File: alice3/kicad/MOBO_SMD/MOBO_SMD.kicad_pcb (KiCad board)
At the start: 2 copper layers, 74.9 x 114.3 mm, 40 parts, among them CON1 SD_Card, P1 CONN_01X05, P2 CONN_01X01, SW1 RESET, SW2 SOFT RESET, U2 VGA_daughter_board, U3 Propeller_P8X32A-D40, U4 24LC256, U5 Propeller_Plug, U6 MiniM4-D40, U8 Z80CPU, U9 KM681000BLP-7, Y1 5 MHz

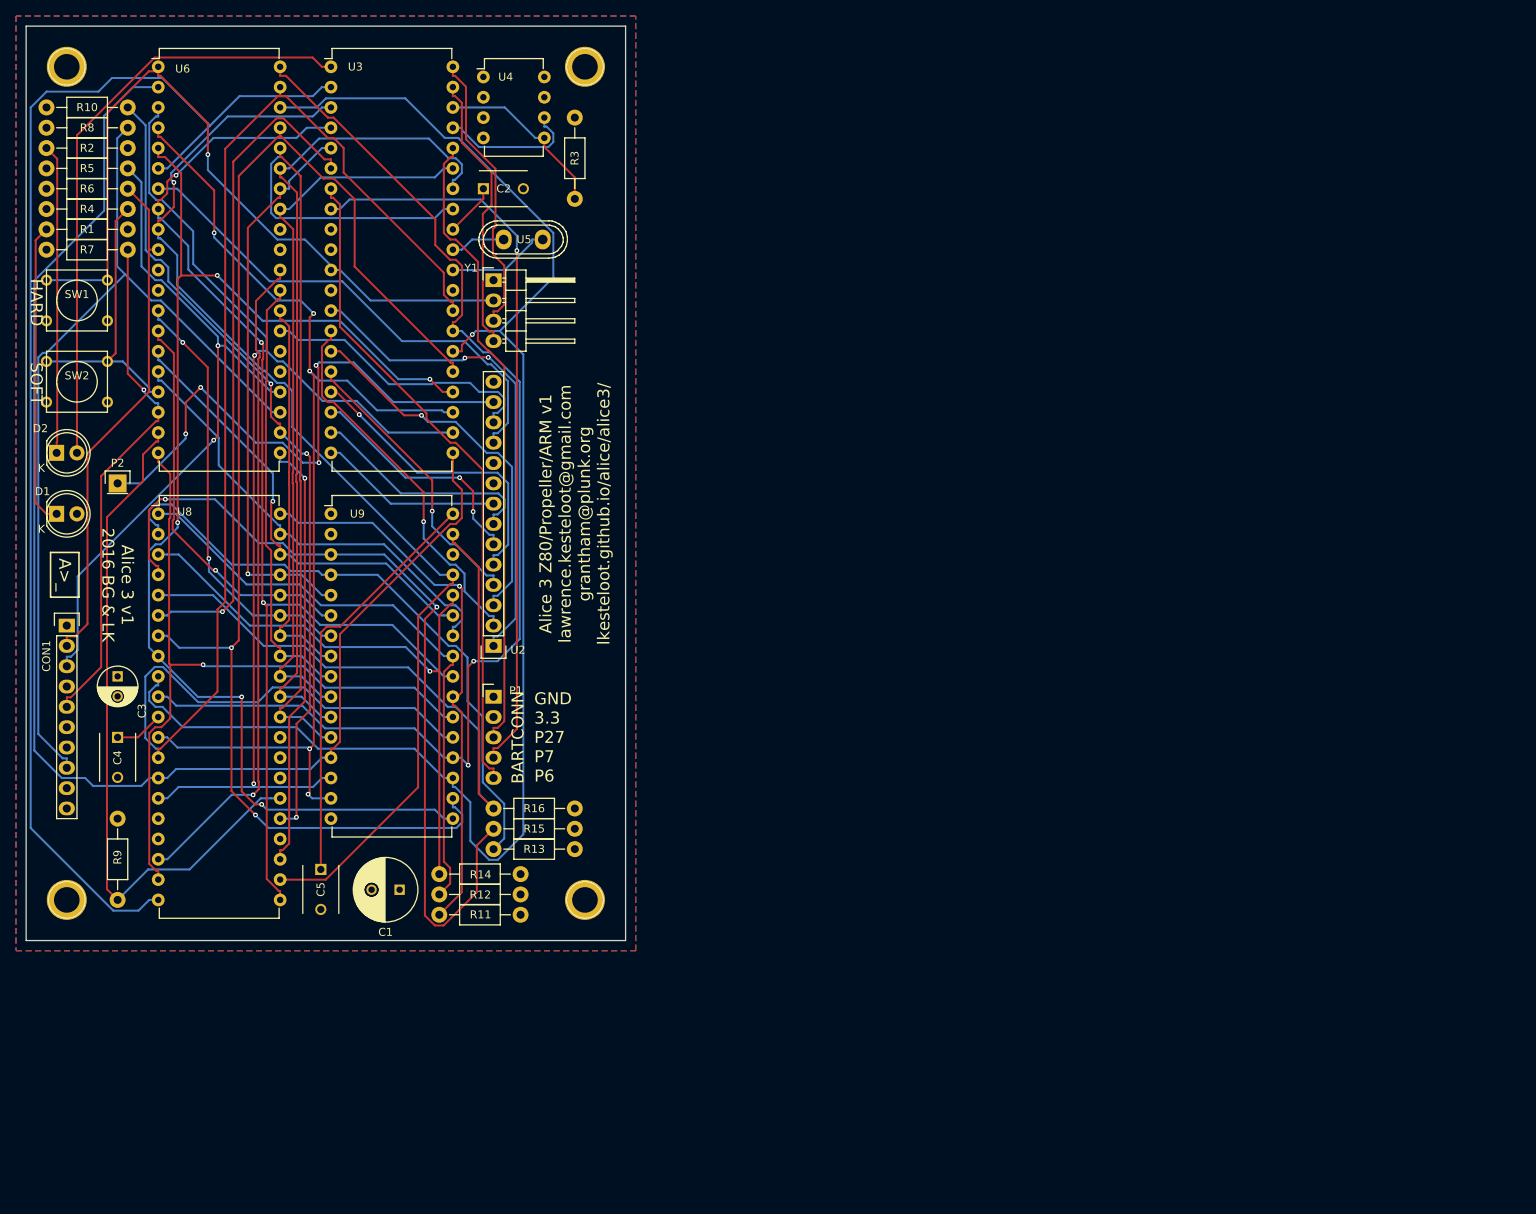
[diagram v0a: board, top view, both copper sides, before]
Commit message: Stab at full PCB
replace DIP36 128KB RAM with TSOP44 512KB RAM
change footprints for many components to SMD
sample PCB layout
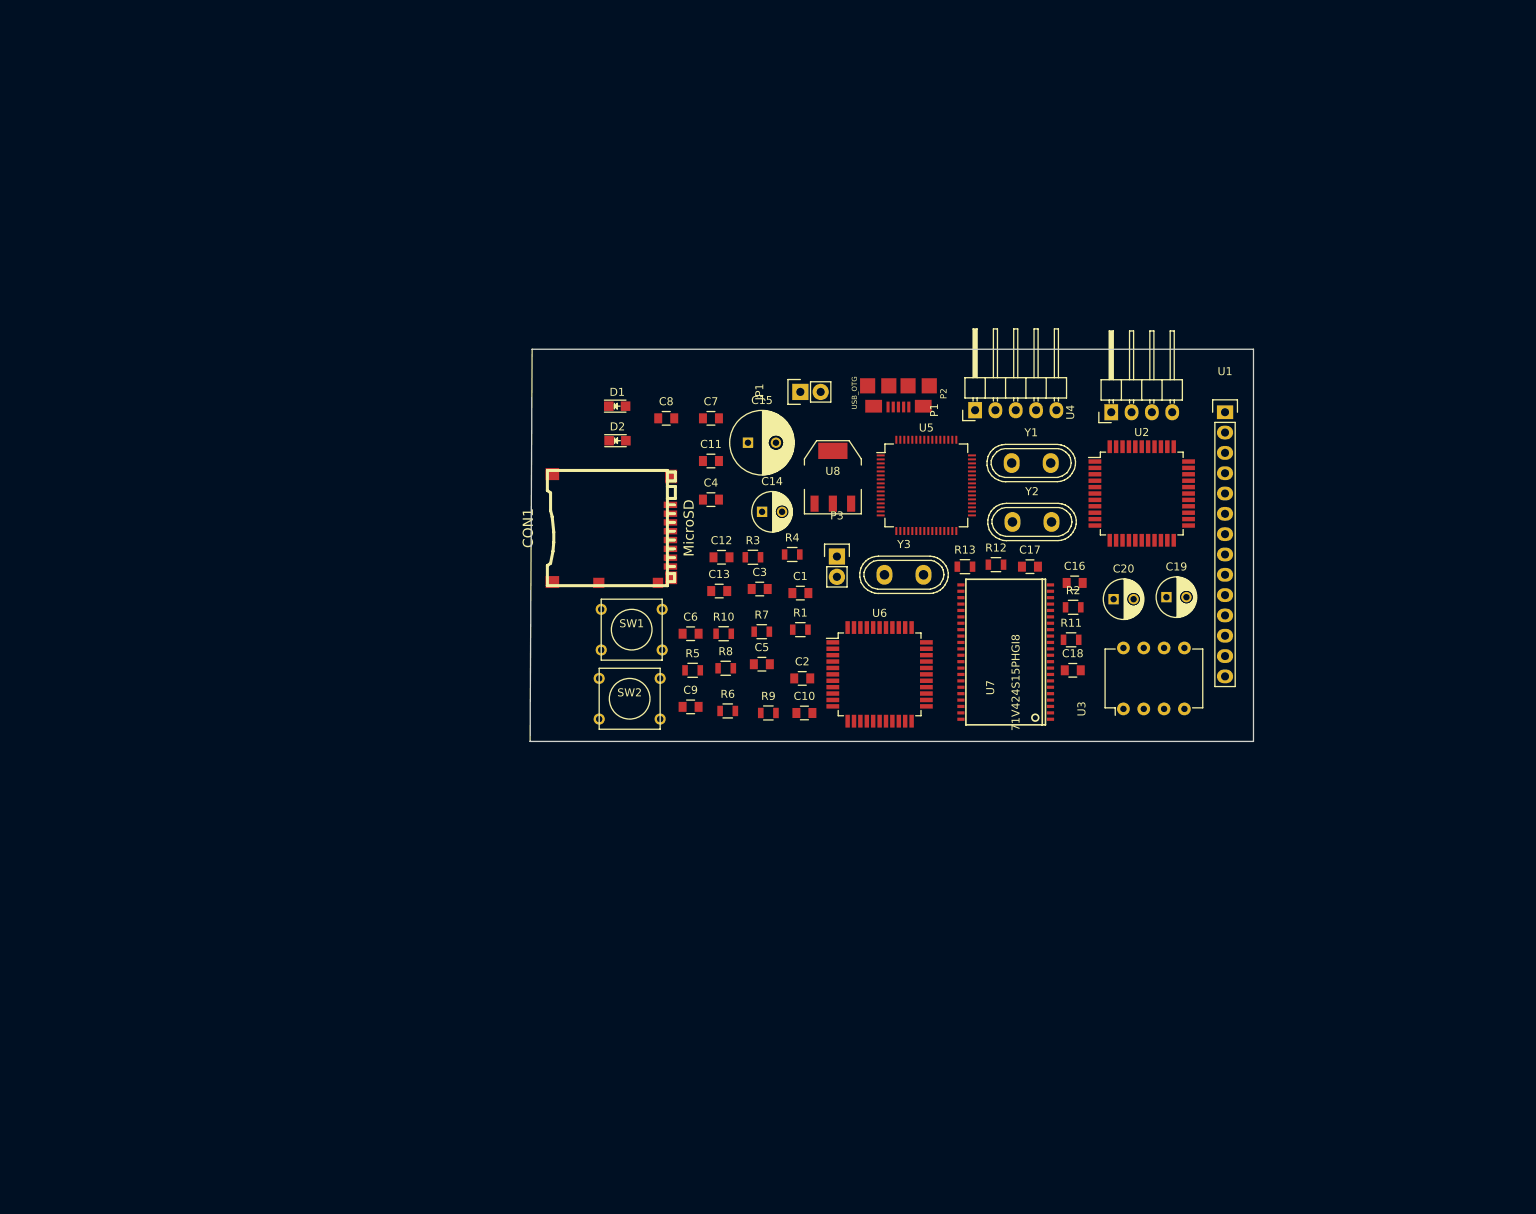
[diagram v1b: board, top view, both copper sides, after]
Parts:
- removed HOLE1, HOLE2, HOLE3, HOLE4: 1pin, Connect:1pin
- removed R14, R15, R16: 10k, Resistors_ThroughHole:Resistor_Horizontal_RM10mm
- removed U9: KM681000BLP-7, Housings_DIP:DIP-32_W15.24mm
- added C10: 2.2µF, Capacitors_SMD:C_0805, F.Cu at (143.0, 118.9)
- added C11: 2.2µF, Capacitors_SMD:C_0805, F.Cu at (131.3, 87.4)
- added C12: 22pF, Capacitors_SMD:C_0805, F.Cu at (132.6, 99.4)
- added C13: 22pF, Capacitors_SMD:C_0805, F.Cu at (132.3, 103.6)
- added C14: 10µF, Capacitors_ThroughHole:C_Radial_D5_L11_P2.5, F.Cu at (137.7, 93.7)
- added C15: 1000 µF, Capacitors_ThroughHole:C_Radial_D8_L11.5_P3.5, F.Cu at (135.9, 85.1)
- added C16: 0.1 µF, Capacitors_SMD:C_0805, F.Cu at (176.8, 102.6)
- added C17: 0.1 µF, Capacitors_SMD:C_0805, F.Cu at (171.2, 100.6)
- added C18: 0.1 µF, Capacitors_SMD:C_0805, F.Cu at (176.5, 113.5)
- added C19: 10µF, Capacitors_ThroughHole:C_Radial_D5_L11_P2.5, F.Cu at (188.3, 104.4)
- added C20: 10µF, Capacitors_ThroughHole:C_Radial_D5_L11_P2.5, F.Cu at (181.7, 104.6)
- added C6: 22pF, Capacitors_SMD:C_0805, F.Cu at (128.8, 109.0)
- added C7: 100nF, Capacitors_SMD:C_0805, F.Cu at (131.3, 82.0)
- added C8: 100nF, Capacitors_SMD:C_0805, F.Cu at (125.7, 82.0)
- added C9: 100nF, Capacitors_SMD:C_0805, F.Cu at (128.8, 118.1)
- added JP1: Jumper_NO_Small, Pin_Headers:Pin_Header_Straight_1x02, F.Cu at (142.5, 78.7)
- added P3: UART1, Pin_Headers:Pin_Header_Straight_1x02, F.Cu at (147.1, 99.3)
- added U1: VGA_daughter_board, Pin_Headers:Pin_Header_Straight_1x14, F.Cu at (195.6, 81.3)
- added U7: 71V424S15PHGI8, TSOP44-II:TSOP44-II, F.Cu at (168.2, 111.3)
- added Y2: 16MHz, Crystals:Crystal_HC50-U_Vertical, F.Cu at (171.4, 95.0)
- added Y3: 32.768KHz, Crystals:Crystal_HC50-U_Vertical, F.Cu at (155.4, 101.6)
- C1: value 1000 µF -> 0.1 µF; footprint Capacitors_ThroughHole:C_Radial_D8_L11.5_P3.5 -> Capacitors_SMD:C_0805
- C2, C4: value 0.1 µF -> 100nF; footprint Capacitors_ThroughHole:C_Disc_D6_P5 -> Capacitors_SMD:C_0805
- C3: value 10µF -> 100nF; footprint Capacitors_ThroughHole:C_Radial_D5_L11_P2.5 -> Capacitors_SMD:C_0805
- C5: value 0.1 µF -> 22pF; footprint Capacitors_ThroughHole:C_Disc_D6_P5 -> Capacitors_SMD:C_0805
- CON1: value SD_Card -> MicroSD; footprint Pin_Headers:Pin_Header_Straight_1x10 -> microsd:microsd_socket
- D1: value POWER -> DEBUG; footprint LEDs:LED-5MM -> LEDs:LED_0805
- D2: value DEBUG -> POWER; footprint LEDs:LED-5MM -> LEDs:LED_0805
- P2: value CONN_01X01 -> USB_OTG; footprint Pin_Headers:Pin_Header_Straight_1x01 -> microusb:10118192-0001LF
- R1, R13, R3, R6, R7, R8: footprint Resistors_ThroughHole:Resistor_Horizontal_RM10mm -> Resistors_SMD:R_0805
- R10: value 1k -> 100; footprint Resistors_ThroughHole:Resistor_Horizontal_RM10mm -> Resistors_SMD:R_0805
- R11, R12: value 10k -> 1k; footprint Resistors_ThroughHole:Resistor_Horizontal_RM10mm -> Resistors_SMD:R_0805
- R2: value 100 -> 10k; footprint Resistors_ThroughHole:Resistor_Horizontal_RM10mm -> Resistors_SMD:R_0805
- R4: value 10k -> 220; footprint Resistors_ThroughHole:Resistor_Horizontal_RM10mm -> Resistors_SMD:R_0805
- R5: value 68K -> 10k; footprint Resistors_ThroughHole:Resistor_Horizontal_RM10mm -> Resistors_SMD:R_0805
- R9: value 1k -> 68K; footprint Resistors_ThroughHole:Resistor_Horizontal_RM10mm -> Resistors_SMD:R_0805
- U2: value VGA_daughter_board -> Propeller_P8X32A-D40; footprint Pin_Headers:Pin_Header_Straight_1x14 -> Housings_QFP:LQFP-44_10x10mm_Pitch0.8mm
- U3: value Propeller_P8X32A-D40 -> 24LC256; footprint Housings_DIP:DIP-40_W15.24mm -> Housings_DIP:DIP-8_W7.62mm
- U4: value 24LC256 -> Propeller_Plug; footprint Housings_DIP:DIP-8_W7.62mm -> Pin_Headers:Pin_Header_Angled_1x04
- U5: value Propeller_Plug -> STM32F415RG; footprint Pin_Headers:Pin_Header_Angled_1x04 -> Housings_QFP:LQFP-64_10x10mm_Pitch0.5mm
- U6: value MiniM4-D40 -> Z80CPU; footprint Housings_DIP:DIP-40_W15.24mm -> Housings_QFP:LQFP-44_10x10mm_Pitch0.8mm
- U8: value Z80CPU -> LD29080DT33R; footprint Housings_DIP:DIP-40_W15.24mm -> TO_SOT_Packages_SMD:SOT-223
- moved R2 136.0 mm to (176.6, 105.7)
- moved U3 127.5 mm to (182.9, 118.4), turned to 90 degrees
- moved U6 117.9 mm to (152.4, 114.0)
- moved R8 104.6 mm to (133.2, 113.3)
- moved R6 103.3 mm to (133.4, 118.6)
- moved R10 103.2 mm to (132.9, 109.0)
- moved R1 102.2 mm to (142.5, 108.5)
- moved P2 98.6 mm to (154.8, 76.5), turned to 180 degrees
- moved R5 98.3 mm to (129.0, 113.5)
- moved R4 98.1 mm to (141.5, 99.1), turned to 0 degrees
- moved R7 96.9 mm to (137.7, 108.7)
- moved U4 89.0 mm to (181.4, 81.3), turned to 90 degrees
- moved U8 84.5 mm to (146.6, 89.4)
- moved R9 83.4 mm to (138.5, 118.9), turned to 0 degrees
- moved U2 83.2 mm to (185.2, 91.4), turned to 0 degrees
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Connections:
- C2 pad 1: +3V3 -> GND
- C2 pad 2: GND -> +3V3
- C3 pad 1: +3V3 -> GND
- C3 pad 2: GND -> +3V3
- C4 pad 1: +3V3 -> GND
- C4 pad 2: GND -> +3V3
- C5 pad 1: +3V3 -> Net-(C5-Pad1)
- CON1 pad 4: Net-(CON1-Pad4) -> +3V3
- CON1 pad 6: +3V3 -> GND
- CON1 pad 7: GND -> /IO/DO
- CON1 pad 8: /IO/DO -> Net-(CON1-Pad8)
- D1 pad 2: +3V3 -> Net-(D1-Pad2)
- D2 pad 2: Net-(D2-Pad2) -> +3V3
- R10 pad 1: +3V3 -> Net-(D2-Pad1)
- R10 pad 2: /BUSRQ -> GND
- R11 pad 1: GND -> /Z80_RESET
- R11 pad 2: A10 -> GND
- R12 pad 1: GND -> +3V3
- R12 pad 2: A11 -> /BUSRQ
- R13 pad 2: A12 -> A16
- R2 pad 1: Net-(D2-Pad1) -> +3V3
- R2 pad 2: GND -> Net-(R2-Pad2)
- R3 pad 2: Net-(R3-Pad2) -> Net-(JP1-Pad1)
- R4 pad 1: Net-(R4-Pad1) -> USB_DET
- R4 pad 2: GND -> +5V
- R5 pad 1: +3V3 -> Net-(R5-Pad1)
- R5 pad 2: /IO/DI -> GND
- R6 pad 2: /IO/CS -> /IO/DO
- R8 pad 2: /IO/DO -> /IO/DI
- R9 pad 1: /Z80_RESET -> +3V3
- R9 pad 2: GND -> /IO/CS
- SW2 pad 1: Net-(R4-Pad1) -> Net-(R5-Pad1)
- U2 pad 1: Net-(U2-Pad1) -> Net-(D1-Pad2)
- U2 pad 10: Net-(U2-Pad10) -> GND
- U2 pad 11: KBD_DATA -> /RESET
- U2 pad 12: KBD_CLK -> +3V3
- U2 pad 13: +5V -> Net-(U1-Pad1)
- U2 pad 14: GND -> Net-(U1-Pad2)
- U2 pad 2: Net-(U2-Pad2) -> /IORQ
- U2 pad 3: Net-(U2-Pad3) -> /WR
- U2 pad 4: Net-(U2-Pad4) -> /RD
- U2 pad 5: Net-(U2-Pad5) -> A7
- U2 pad 6: Net-(U2-Pad6) -> CLK
- U2 pad 7: Net-(U2-Pad7) -> Net-(P1-Pad5)
- U2 pad 8: Net-(U2-Pad8) -> Net-(P1-Pad4)
- U2 pad 9: Net-(U2-Pad9) -> GND
- U3 pad 1: Net-(D2-Pad2) -> GND
- U3 pad 2: /IORQ -> GND
- U3 pad 3: /WR -> GND
- U3 pad 4: /RD -> GND
- U3 pad 5: A7 -> Net-(R2-Pad2)
- U3 pad 6: CLK -> Net-(U2-Pad37)
- U3 pad 7: Net-(P1-Pad5) -> GND
- U3 pad 8: Net-(P1-Pad4) -> +3V3
- U4 pad 2: GND -> /RESET
- U4 pad 3: GND -> Net-(U2-Pad40)
- U4 pad 4: GND -> Net-(U2-Pad39)
- U5 pad 1: GND -> +3V3
- U5 pad 2: /RESET -> A10
- U5 pad 3: Net-(U3-Pad40) -> Net-(C12-Pad1)
- U5 pad 4: Net-(U3-Pad39) -> Net-(C13-Pad2)
- U6 pad 1: /RESET -> A11
- U6 pad 10: /IO/CS -> D6
- U6 pad 12: GND -> D2
- U6 pad 13: A5 -> D7
- U6 pad 14: A6 -> D0
- U6 pad 15: A8 -> D1
- U6 pad 16: A9 -> +3V3
- U6 pad 17: Net-(R4-Pad1) -> +3V3
- U6 pad 18: /IO/SCK -> /HALT
- U6 pad 19: /Z80_RESET -> /MREQ
- U6 pad 2: D0 -> A12
- U6 pad 20: /MREQ -> /IORQ
- U6 pad 21: /BUSACK -> /RD
- U6 pad 22: /BUSRQ -> /WR
- U6 pad 23: /IO/DO -> /BUSACK
- U6 pad 24: /IO/DI -> +3V3
- U6 pad 25: Net-(U6-Pad25) -> /BUSRQ
- U6 pad 26: Net-(U6-Pad26) -> /Z80_RESET
- U6 pad 27: KBD_CLK -> Net-(U6-Pad27)
- U6 pad 28: A4 -> Net-(U6-Pad28)
- U6 pad 29: A3 -> GND
- U6 pad 3: D1 -> A13
- U6 pad 30: /HALT -> A0
- U6 pad 31: GND -> A1
- U6 pad 32: +3V3 -> A2
- U6 pad 33: A2 -> A3
- U6 pad 34: A7 -> A4
- U6 pad 35: A1 -> A5
- U6 pad 36: A0 -> A6
- U6 pad 37: D4 -> A7
- U6 pad 38: D5 -> A8
- U6 pad 39: D7 -> A9
- U6 pad 4: D2 -> A14
- U6 pad 40: D6 -> A10
- U6 pad 5: D3 -> A15
- U6 pad 6: /IORQ -> CLK
- U6 pad 7: KBD_DATA -> D4
- U6 pad 8: /RD -> D3
- U6 pad 9: /WR -> D5
- U8 pad 1: A11 -> +5V
- U8 pad 2: A12 -> GND
- U8 pad 3: A13 -> +3V3
- U8 pad 4: A14 -> (no net)
- Y1 pad 1: Net-(U3-Pad30) -> Net-(U2-Pad30)
- Y1 pad 2: Net-(U3-Pad31) -> Net-(U2-Pad31)
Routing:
- net D5: track 191.6 -> 0.00 mm, vias 1 -> 0
- net D7: track 182.3 -> 0.00 mm
- net D0: track 177.5 -> 0.00 mm
- net D4: track 169.5 -> 0.00 mm, vias 2 -> 0
- net /IORQ: track 163.0 -> 0.00 mm
- net D3: track 160.0 -> 0.00 mm, vias 5 -> 0
- net D6: track 150.1 -> 0.00 mm, vias 2 -> 0
- net /RD: track 147.9 -> 0.00 mm, vias 3 -> 0
- net D1: track 143.4 -> 0.00 mm, vias 2 -> 0
- net /WR: track 142.3 -> 0.00 mm, vias 1 -> 0
- net D2: track 136.6 -> 0.00 mm, vias 5 -> 0
- net /IO/DO: track 114.2 -> 0.00 mm
- net A0: track 113.2 -> 0.00 mm
- net A14: track 107.5 -> 0.00 mm, vias 2 -> 0
- net A1: track 104.8 -> 0.00 mm
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- removed copper zone on F.Cu, net +3V3
- removed copper zone on B.Cu, net GND
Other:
- board size 74.9 x 114.3 mm -> 90.4 x 49 mm
- board text removed: "A>_"
- board text removed: "Alice 3 Z80/Propeller/ARM v1 lawrence.kesteloot@gmail.com grantham@plunk.org lkesteloot.github.io/alice/alice3/"
- board text removed: "Alice 3 v1 2016 BG & LK"
- board text removed: "BARTCONN"
- board text removed: "GND 3.3 P27 P7 P6"
- board text removed: "HARD"
- board text removed: "SOFT"

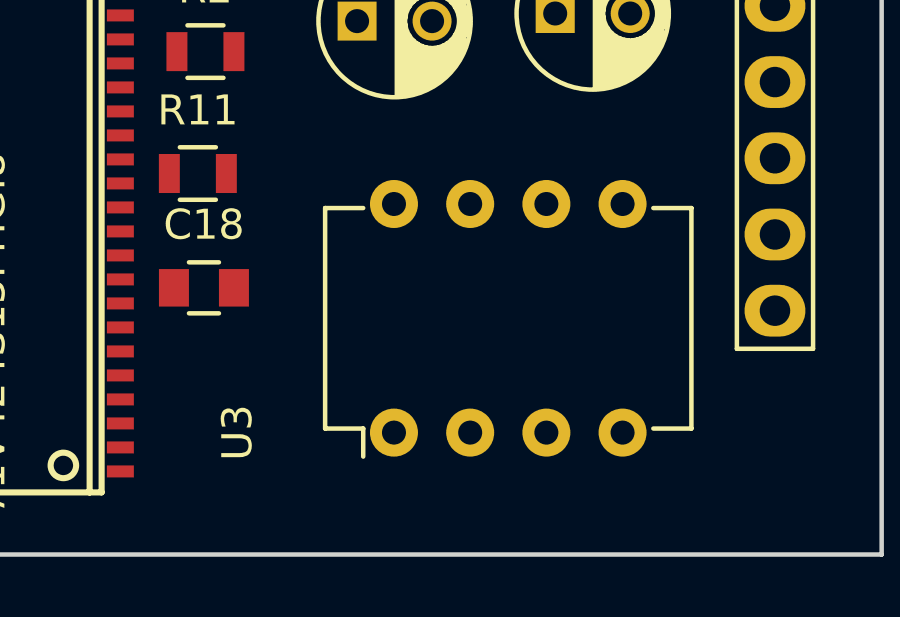
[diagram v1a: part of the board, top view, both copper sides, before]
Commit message: switch Propeller ROM to SOIC8
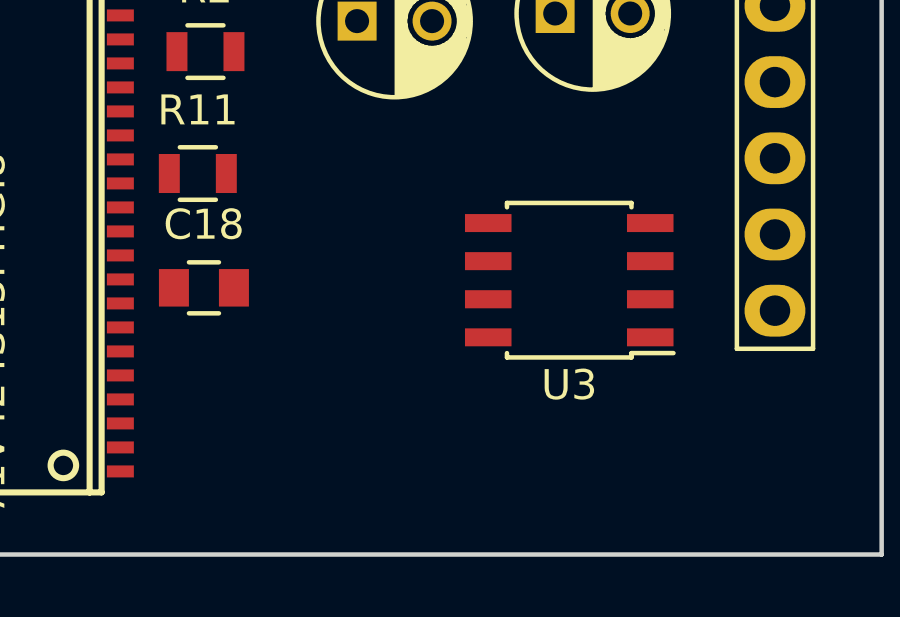
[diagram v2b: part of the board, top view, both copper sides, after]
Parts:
- U3: footprint Housings_DIP:DIP-8_W7.62mm -> Housings_SOIC:SOIC-8_3.9x4.9mm_Pitch1.27mm
- moved U3 7.74 mm to (188.7, 113.3), turned to 180 degrees
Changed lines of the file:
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@@
     (links 229)
     (no_connects 229)
-    (area 0 0 0 0)
+    (area 108.636999 73.330999 199.211001 122.503001)
     (thickness 1.6)
     (drawings 4)
@@
     )
   )
-  (module Housings_DIP:DIP-8_W7.62mm (layer F.Cu)
-    (at 182.88 118.364 90)
-    (descr "8-lead dip package, row spacing 7.62 mm (300 mils)")
-    (tags "dil dip 2.54 300")
-    (fp_text reference U3 (at 0 -5.22 90) (layer F.SilkS)
-      (effects (font (size 1 1) (thickness 0.15)))
-    )
-    (fp_text value 24LC256 (at 0 -3.72 90) (layer F.Fab)
-      (effects (font (size 1 1) (thickness 0.15)))
-    )
-    (fp_line (start -1.05 -2.45) (end -1.05 10.1) (layer F.CrtYd) (width 0.05))
-    (fp_line (start 8.65 -2.45) (end 8.65 10.1) (layer F.CrtYd) (width 0.05))
-    (fp_line (start -1.05 -2.45) (end 8.65 -2.45) (layer F.CrtYd) (width 0.05))
-    (fp_line (start -1.05 10.1) (end 8.65 10.1) (layer F.CrtYd) (width 0.05))
-    (fp_line (start 0.135 -2.295) (end 0.135 -1.025) (layer F.SilkS) (width 0.15))
-    (fp_line (start 7.485 -2.295) (end 7.485 -1.025) (layer F.SilkS) (width 0.15))
-    (fp_line (start 7.485 9.915) (end 7.485 8.645) (layer F.SilkS) (width 0.15))
-    (fp_line (start 0.135 9.915) (end 0.135 8.645) (layer F.SilkS) (width 0.15))
-    (fp_line (start 0.135 -2.295) (end 7.485 -2.295) (layer F.SilkS) (width 0.15))
-    (fp_line (start 0.135 9.915) (end 7.485 9.915) (layer F.SilkS) (width 0.15))
-    (fp_line (start 0.135 -1.025) (end -0.8 -1.025) (layer F.SilkS) (width 0.15))
-    (pad 1 thru_hole oval (at 0 0 90) (size 1.6 1.6) (drill 0.8) (layers *.Cu *.Mask F.SilkS)
-      (net 2 GND))
-    (pad 2 thru_hole oval (at 0 2.54 90) (size 1.6 1.6) (drill 0.8) (layers *.Cu *.Mask F.SilkS)
-      (net 2 GND))
-    (pad 3 thru_hole oval (at 0 5.08 90) (size 1.6 1.6) (drill 0.8) (layers *.Cu *.Mask F.SilkS)
-      (net 2 GND))
-    (pad 4 thru_hole oval (at 0 7.62 90) (size 1.6 1.6) (drill 0.8) (layers *.Cu *.Mask F.SilkS)
-      (net 2 GND))
-    (pad 5 thru_hole oval (at 7.62 7.62 90) (size 1.6 1.6) (drill 0.8) (layers *.Cu *.Mask F.SilkS)
-      (net 28 "Net-(R2-Pad2)"))
-    (pad 6 thru_hole oval (at 7.62 5.08 90) (size 1.6 1.6) (drill 0.8) (layers *.Cu *.Mask F.SilkS)
-      (net 65 "Net-(U2-Pad37)"))
-    (pad 7 thru_hole oval (at 7.62 2.54 90) (size 1.6 1.6) (drill 0.8) (layers *.Cu *.Mask F.SilkS)
-      (net 2 GND))
-    (pad 8 thru_hole oval (at 7.62 0 90) (size 1.6 1.6) (drill 0.8) (layers *.Cu *.Mask F.SilkS)
-      (net 1 +3V3))
-    (model Housings_DIP.3dshapes/DIP-8_W7.62mm.wrl
-      (at (xyz 0 0 0))
-      (scale (xyz 1 1 1))
-      (rotate (xyz 0 0 0))
-    )
-  )
   (module Pin_Headers:Pin_Header_Angled_1x04 (layer F.Cu)
     (at 181.356 81.28 90)
@@
       (net 9 "Net-(C13-Pad2)"))
   )
+  (module Housings_SOIC:SOIC-8_3.9x4.9mm_Pitch1.27mm (layer F.Cu)
+    (at 188.722 113.284 180)
+    (descr "8-Lead Plastic Small Outline (SN) - Narrow, 3.90 mm Body [SOIC] (see Microchip Packaging Specification 00000049BS.pdf)")
+    (tags "SOIC 1.27")
+    (attr smd)
+    (fp_text reference U3 (at 0 -3.5 180) (layer F.SilkS)
+      (effects (font (size 1 1) (thickness 0.15)))
+    )
+    (fp_text value 24LC256 (at 0 3.5 180) (layer F.Fab)
+      (effects (font (size 1 1) (thickness 0.15)))
+    )
+    (fp_line (start -3.75 -2.75) (end -3.75 2.75) (layer F.CrtYd) (width 0.05))
+    (fp_line (start 3.75 -2.75) (end 3.75 2.75) (layer F.CrtYd) (width 0.05))
+    (fp_line (start -3.75 -2.75) (end 3.75 -2.75) (layer F.CrtYd) (width 0.05))
+    (fp_line (start -3.75 2.75) (end 3.75 2.75) (layer F.CrtYd) (width 0.05))
+    (fp_line (start -2.075 -2.575) (end -2.075 -2.43) (layer F.SilkS) (width 0.15))
+    (fp_line (start 2.075 -2.575) (end 2.075 -2.43) (layer F.SilkS) (width 0.15))
+    (fp_line (start 2.075 2.575) (end 2.075 2.43) (layer F.SilkS) (width 0.15))
+    (fp_line (start -2.075 2.575) (end -2.075 2.43) (layer F.SilkS) (width 0.15))
+    (fp_line (start -2.075 -2.575) (end 2.075 -2.575) (layer F.SilkS) (width 0.15))
+    (fp_line (start -2.075 2.575) (end 2.075 2.575) (layer F.SilkS) (width 0.15))
+    (fp_line (start -2.075 -2.43) (end -3.475 -2.43) (layer F.SilkS) (width 0.15))
+    (pad 1 smd rect (at -2.7 -1.905 180) (size 1.55 0.6) (layers F.Cu F.Paste F.Mask)
+      (net 2 GND))
+    (pad 2 smd rect (at -2.7 -0.635 180) (size 1.55 0.6) (layers F.Cu F.Paste F.Mask)
+      (net 2 GND))
+    (pad 3 smd rect (at -2.7 0.635 180) (size 1.55 0.6) (layers F.Cu F.Paste F.Mask)
+      (net 2 GND))
+    (pad 4 smd rect (at -2.7 1.905 180) (size 1.55 0.6) (layers F.Cu F.Paste F.Mask)
+      (net 2 GND))
+    (pad 5 smd rect (at 2.7 1.905 180) (size 1.55 0.6) (layers F.Cu F.Paste F.Mask)
+      (net 28 "Net-(R2-Pad2)"))
+    (pad 6 smd rect (at 2.7 0.635 180) (size 1.55 0.6) (layers F.Cu F.Paste F.Mask)
+      (net 65 "Net-(U2-Pad37)"))
+    (pad 7 smd rect (at 2.7 -0.635 180) (size 1.55 0.6) (layers F.Cu F.Paste F.Mask)
+      (net 2 GND))
+    (pad 8 smd rect (at 2.7 -1.905 180) (size 1.55 0.6) (layers F.Cu F.Paste F.Mask)
+      (net 1 +3V3))
+    (model Housings_SOIC.3dshapes/SOIC-8_3.9x4.9mm_Pitch1.27mm.wrl
+      (at (xyz 0 0 0))
+      (scale (xyz 1 1 1))
+      (rotate (xyz 0 0 0))
+    )
+  )
   (gr_line (start 199.136 73.406) (end 108.966 73.406) (layer Edge.Cuts) (width 0.15))
